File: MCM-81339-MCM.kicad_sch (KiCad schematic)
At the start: 35 parts, among them J3 Conn_02x03_Odd_Even, J5 USB_B_Mini, U5 ESP32-S3-WROOM-2

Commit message: apply updates as per changelog.md
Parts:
- R26: value 100k -> 87k6
- R27: value 100k -> 110k
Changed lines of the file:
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@@
       (effects (font (size 1.27 1.27)) (justify left))
     )
-    (property "Value" "100k" (at 72.39 171.4499 0)
+    (property "Value" "110k" (at 72.39 171.4499 0)
       (effects (font (size 1.27 1.27)) (justify left))
     )
@@
       (effects (font (size 1.27 1.27)) (justify left))
     )
-    (property "Value" "100k" (at 72.39 161.2899 0)
-      (effects (font (size 1.27 1.27)) (justify left))
-    )
+    (property "Value" "87k6" (at 72.39 161.2899 0)
+      (effects (font (size 1.27 1.27)) (justify left))
+    )

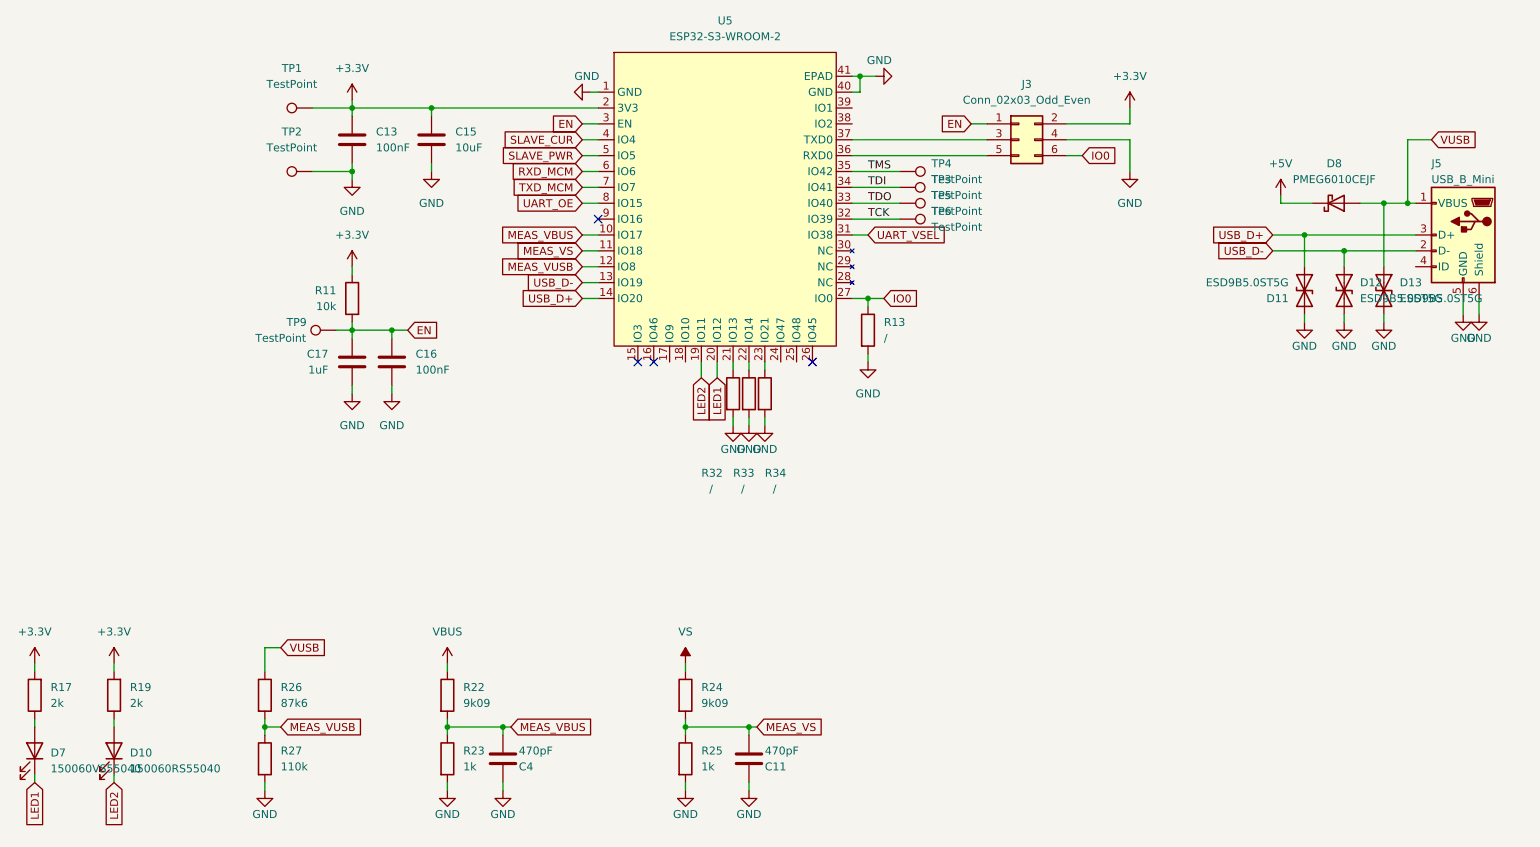
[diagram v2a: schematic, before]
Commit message: Updates for v1.3
* Update: ESP to ESP32-S3-WROOM-1-N16R8
* Add: optional 2k2 pull up on IO7 for debug purposes
* Add: optional 220pF cap on IO6 for debug purposes
* Update: USB connector to C type
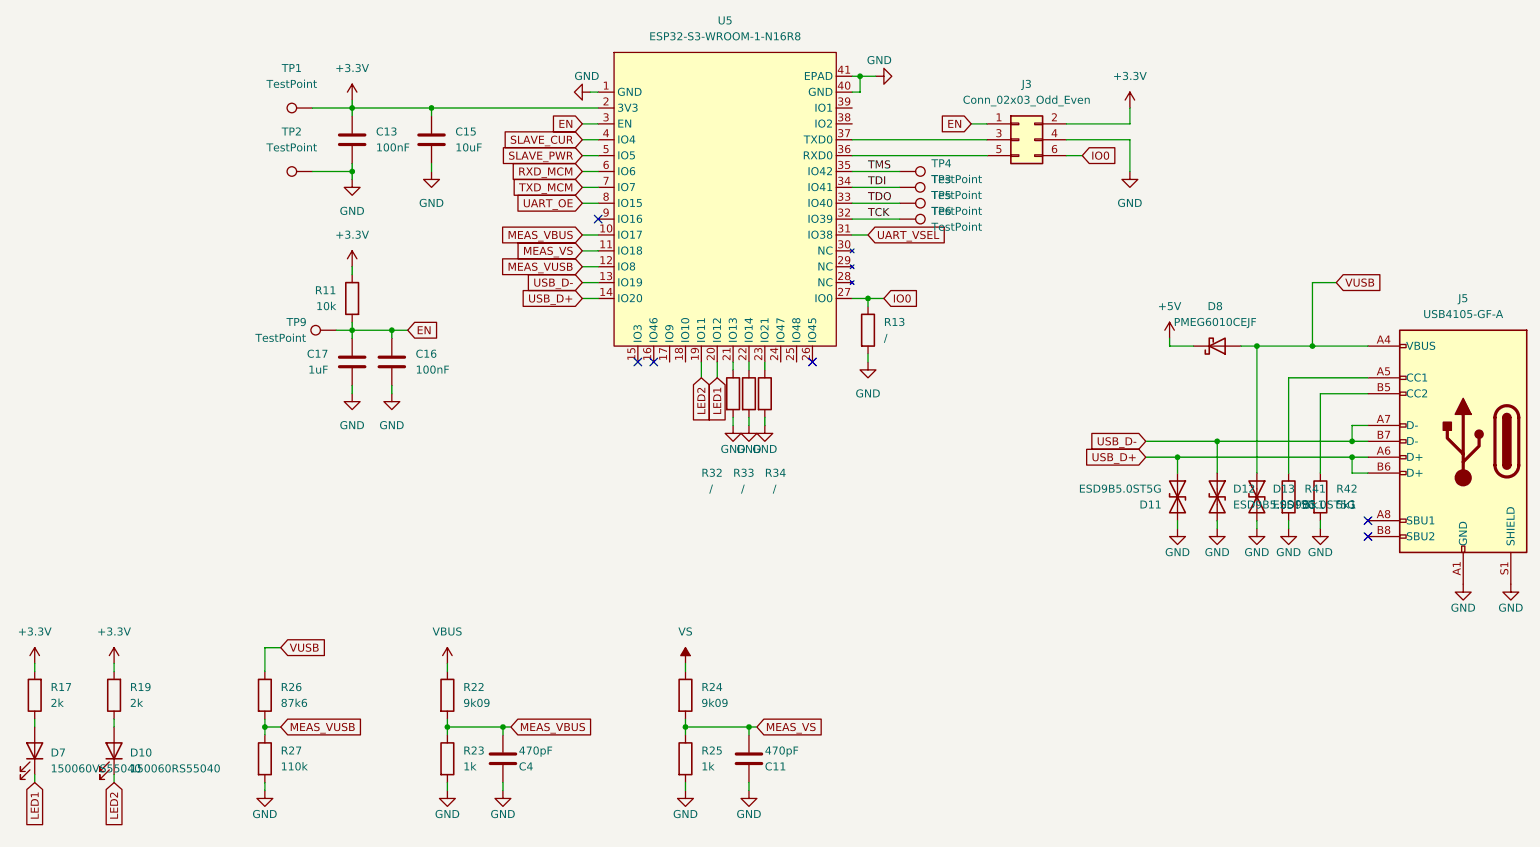
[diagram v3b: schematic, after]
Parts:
- removed J5: USB_B_Mini, Connector_USB:USB_Mini-B_Wuerth_65100516121_Horizontal, symbol Connector:USB_B_Mini
- added J5: USB4105-GF-A, Connector_USB:USB_C_Receptacle_GCT_USB4105-xx-A_16P_TopMnt_Horizontal, symbol Connector:USB_C_Receptacle_USB2.0_16P
- added R41, R42: 5k1, Resistor_SMD:R_0402_1005Metric, symbol Device:R
- U5: value ESP32-S3-WROOM-2 -> ESP32-S3-WROOM-1-N16R8
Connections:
- net GND: now also J5.A1 (GND), J5.A12 (GND), J5.B1 (GND), J5.B12 (GND), J5.S1 (SHIELD), R41.2, R42.2
- net USB_D+: now also J5.A6 (D+), J5.B6 (D+)
- net USB_D-: now also J5.A7 (D-), J5.B7 (D-)
- net VUSB: now also J5.A4 (VBUS), J5.A9 (VBUS), J5.B4 (VBUS), J5.B9 (VBUS)
- new net: J5.B5 (CC2), R42.1
- new net: J5.A5 (CC1), R41.1
- no-connect marks 4 -> 6
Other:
- moved on the sheet: D11, D12, D13, D8

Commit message: prepare next devs
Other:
- company: (none) -> Melexis
- title: (none) -> MCM-81339
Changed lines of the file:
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@@
 	(generator_version "9.0")
 	(paper "A4")
+	(title_block
+		(title "MCM-81339")
+		(date "2026-01-28")
+		(rev "v1.5")
+		(company "Melexis")
+	)
 	(junction
 		(at 165.1 60.96)
